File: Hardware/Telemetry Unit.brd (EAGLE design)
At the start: 50.8 x 63.5 mm, 38 parts, among them IC1 MEGA128-A, Q1 10MHz, U1 MPL3115A2, U2 AP65111A, U3 LSM6DS3

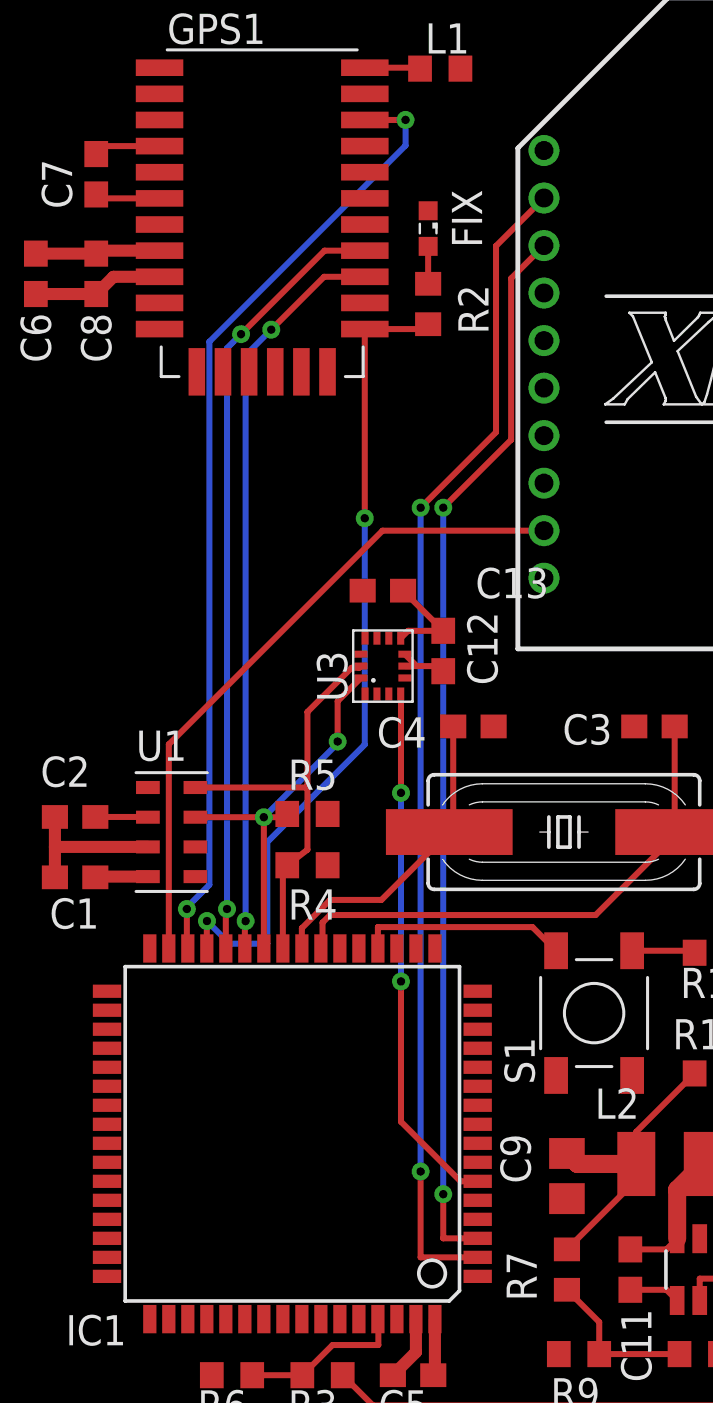
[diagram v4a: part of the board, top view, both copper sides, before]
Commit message: Apparently hadn't completely saved
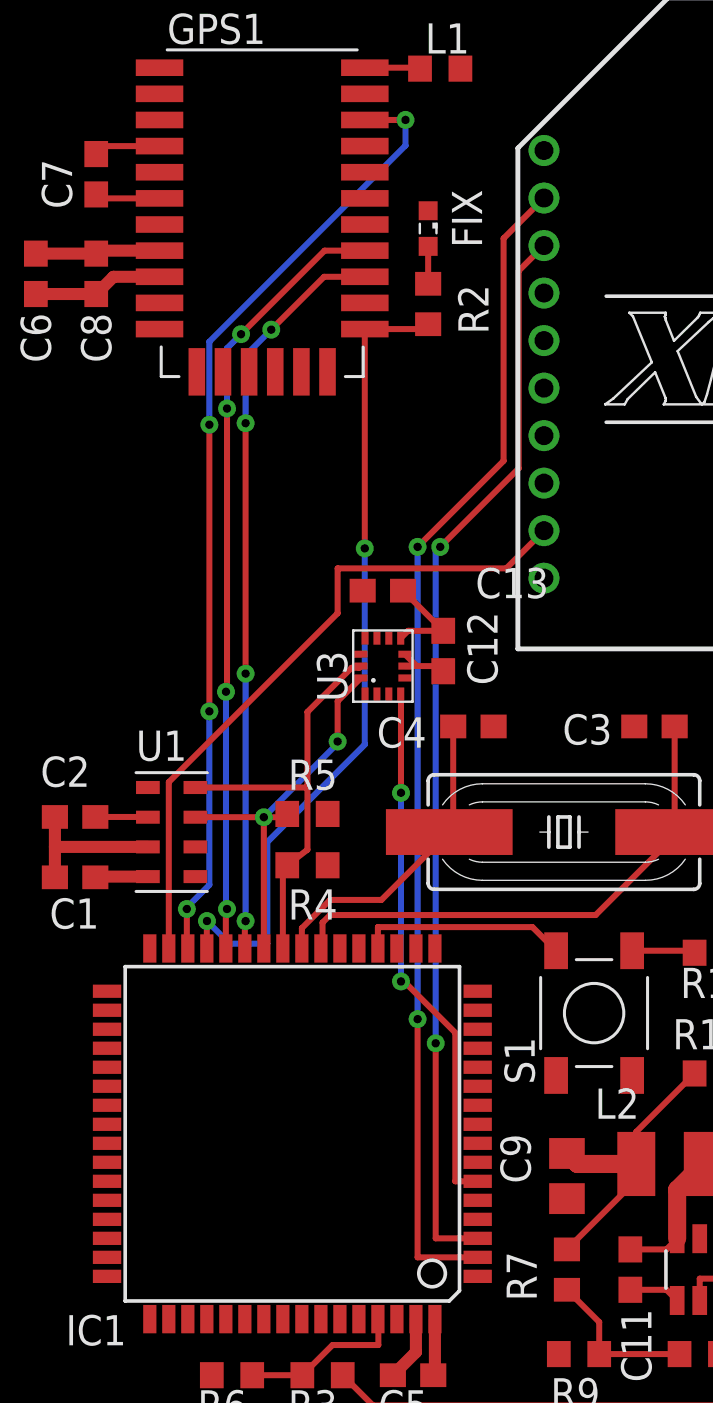
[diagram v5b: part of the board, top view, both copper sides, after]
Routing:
- net TX1: track 32.8 -> 32.9 mm, vias 2 -> 4
- net RX1: vias 2 -> 4
- net !GPS_SLP: vias 2 -> 4
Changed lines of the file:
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@@
 <contactref element="IC1" pad="2"/>
 <contactref element="XB1" pad="2"/>
-<wire x1="20.5" y1="10.04" x2="18.0975" y2="10.04" width="0.254" layer="1"/>
-<wire x1="18.0975" y1="10.04" x2="18.0975" y2="13.6525" width="0.254" layer="1"/>
-<via x="18.0975" y="13.6525" extent="1-16" drill="0.35"/>
-<wire x1="18.0975" y1="13.6525" x2="18.0975" y2="41.5925" width="0.254" layer="16"/>
-<via x="18.0975" y="41.5925" extent="1-16" drill="0.35"/>
-<wire x1="18.0975" y1="41.5925" x2="21.2725" y2="44.7675" width="0.254" layer="1"/>
-<wire x1="21.2725" y1="52.6075" x2="23.29" y2="54.625" width="0.254" layer="1"/>
-<wire x1="21.2725" y1="44.7675" x2="21.2725" y2="52.6075" width="0.254" layer="1"/>
+<wire x1="20.5" y1="10.04" x2="17.9705" y2="10.04" width="0.254" layer="1"/>
+<wire x1="17.9705" y1="10.04" x2="17.9705" y2="20.066" width="0.254" layer="1"/>
+<via x="17.9705" y="20.066" extent="1-16" drill="0.35"/>
+<wire x1="17.9705" y1="39.9415" x2="17.9705" y2="20.066" width="0.254" layer="16"/>
+<via x="17.9705" y="39.9415" extent="1-16" drill="0.35"/>
+<wire x1="17.9705" y1="39.9415" x2="21.59" y2="43.561" width="0.254" layer="1"/>
+<wire x1="21.59" y1="52.925" x2="23.29" y2="54.625" width="0.254" layer="1"/>
+<wire x1="21.59" y1="43.561" x2="21.59" y2="52.925" width="0.254" layer="1"/>
 </signal>
 <signal name="TX0">
 <contactref element="IC1" pad="3"/>
 <contactref element="XB1" pad="3"/>
-<wire x1="20.5" y1="10.84" x2="19.05" y2="10.84" width="0.254" layer="1"/>
-<wire x1="19.05" y1="10.84" x2="19.05" y2="12.7" width="0.254" layer="1"/>
-<via x="19.05" y="12.7" extent="1-16" drill="0.35"/>
-<wire x1="19.05" y1="12.7" x2="19.05" y2="41.5925" width="0.254" layer="16"/>
-<via x="19.05" y="41.5925" extent="1-16" drill="0.35"/>
-<wire x1="19.05" y1="41.5925" x2="21.9075" y2="44.45" width="0.254" layer="1"/>
-<wire x1="21.9075" y1="51.2425" x2="23.29" y2="52.625" width="0.254" layer="1"/>
-<wire x1="21.9075" y1="44.45" x2="21.9075" y2="51.2425" width="0.254" layer="1"/>
+<wire x1="20.5" y1="10.84" x2="18.7325" y2="10.84" width="0.254" layer="1"/>
+<wire x1="18.7325" y1="10.84" x2="18.7325" y2="19.05" width="0.254" layer="1"/>
+<via x="18.7325" y="19.05" extent="1-16" drill="0.35"/>
+<wire x1="18.7325" y1="39.751" x2="18.923" y2="39.9415" width="0.254" layer="16"/>
+<wire x1="18.7325" y1="39.751" x2="18.7325" y2="19.05" width="0.254" layer="16"/>
+<via x="18.923" y="39.9415" extent="1-16" drill="0.35"/>
+<wire x1="18.923" y1="39.9415" x2="22.225" y2="43.2435" width="0.254" layer="1"/>
+<wire x1="22.225" y1="51.56" x2="23.29" y2="52.625" width="0.254" layer="1"/>
+<wire x1="22.225" y1="43.2435" x2="22.225" y2="51.56" width="0.254" layer="1"/>
 </signal>
 <signal name="SCK">
@@
 <wire x1="9.9" y1="24.7015" x2="9.949815625" y2="24.7015" width="0.254" layer="1"/>
 <via x="9.949815625" y="24.7015" extent="1-16" drill="0.35"/>
-<wire x1="9.949815625" y1="24.7015" x2="9.949815625" y2="48.303815625" width="0.254" layer="16"/>
-<wire x1="9.949815625" y1="48.303815625" x2="10.541" y2="48.895" width="0.254" layer="16"/>
+<wire x1="9.949815625" y1="24.7015" x2="9.906" y2="24.745315625" width="0.254" layer="16"/>
+<wire x1="9.906" y1="24.745315625" x2="9.906" y2="33.8455" width="0.254" layer="16"/>
+<wire x1="10.541" y1="48.895" x2="9.949815625" y2="48.303815625" width="0.254" layer="16"/>
+<wire x1="9.949815625" y1="48.303815625" x2="9.949815625" y2="45.763815625" width="0.254" layer="16"/>
 <via x="10.541" y="48.895" extent="1-16" drill="0.35"/>
 <wire x1="10.541" y1="48.895" x2="14.056" y2="52.41" width="0.254" layer="1"/>
 <wire x1="14.056" y1="52.41" x2="15.75" y2="52.41" width="0.254" layer="1"/>
+<via x="9.906" y="33.8455" extent="1-16" drill="0.35"/>
+<via x="9.949815625" y="45.763815625" extent="1-16" drill="0.35"/>
+<wire x1="9.949815625" y1="45.763815625" x2="9.949815625" y2="33.889315625" width="0.254" layer="1"/>
+<wire x1="9.949815625" y1="33.889315625" x2="9.906" y2="33.8455" width="0.254" layer="1"/>
 </signal>
 <signal name="RX1">
@@
 <wire x1="10.7" y1="24.1935" x2="10.7315" y2="24.1935" width="0.254" layer="1"/>
 <via x="10.7315" y="24.1935" extent="1-16" drill="0.35"/>
-<wire x1="10.7315" y1="24.1935" x2="10.7315" y2="48.006" width="0.254" layer="16"/>
-<wire x1="10.7315" y1="48.006" x2="11.811" y2="49.0855" width="0.254" layer="16"/>
+<wire x1="10.7315" y1="24.1935" x2="10.7315" y2="34.6075" width="0.254" layer="16"/>
+<wire x1="10.7315" y1="34.6075" x2="10.7315" y2="45.1485" width="0.254" layer="1"/>
+<wire x1="11.811" y1="49.0855" x2="10.7315" y2="48.006" width="0.254" layer="16"/>
+<wire x1="10.7315" y1="48.006" x2="10.7315" y2="45.1485" width="0.254" layer="16"/>
 <via x="11.811" y="49.0855" extent="1-16" drill="0.35"/>
 <wire x1="15.75" y1="51.31" x2="14.0355" y2="51.31" width="0.254" layer="1"/>
 <wire x1="14.0355" y1="51.31" x2="11.811" y2="49.0855" width="0.254" layer="1"/>
+<via x="10.7315" y="34.6075" extent="1-16" drill="0.35"/>
+<via x="10.7315" y="45.1485" extent="1-16" drill="0.35"/>
 </signal>
 <signal name="MOSI">
@@
 <wire x1="11.6444" y1="23.241" x2="10.0569" y2="23.241" width="0.254" layer="16"/>
 <wire x1="9.1044" y1="24.1935" x2="10.0569" y2="23.241" width="0.254" layer="16"/>
-<wire x1="15.748" y1="31.623" x2="15.748" y2="41.148" width="0.254" layer="16"/>
-<via x="15.748" y="41.148" extent="1-16" drill="0.35"/>
+<wire x1="15.748" y1="31.623" x2="15.748" y2="39.878" width="0.254" layer="16"/>
+<via x="15.748" y="39.878" extent="1-16" drill="0.35"/>
 <wire x1="15.75" y1="49.11" x2="15.748" y2="49.108" width="0.254" layer="1"/>
-<wire x1="15.748" y1="49.108" x2="15.748" y2="41.148" width="0.254" layer="1"/>
+<wire x1="15.748" y1="49.108" x2="15.748" y2="39.878" width="0.254" layer="1"/>
 <wire x1="15.75" y1="49.11" x2="18.21" y2="49.11" width="0.254" layer="1"/>
 <wire x1="18.21" y1="49.11" x2="18.415" y2="49.315" width="0.254" layer="1"/>
@@
 <wire x1="8.2591" y1="24.7015" x2="8.2591" y2="24.7691" width="0.254" layer="16"/>
 <wire x1="8.2591" y1="24.7691" x2="9.2075" y2="25.7175" width="0.254" layer="16"/>
-<wire x1="9.2075" y1="25.7175" x2="9.2075" y2="48.5775" width="0.254" layer="16"/>
-<wire x1="9.2075" y1="48.5775" x2="17.4625" y2="56.8325" width="0.254" layer="16"/>
+<wire x1="9.2075" y1="25.7175" x2="9.2075" y2="33.02" width="0.254" layer="16"/>
+<wire x1="9.2075" y1="33.02" x2="9.2075" y2="45.085" width="0.254" layer="1"/>
+<wire x1="17.4625" y1="56.8325" x2="9.2075" y2="48.5775" width="0.254" layer="16"/>
+<wire x1="9.2075" y1="45.085" x2="9.2075" y2="48.5775" width="0.254" layer="16"/>
 <wire x1="17.4625" y1="56.8325" x2="17.4625" y2="57.912" width="0.254" layer="16"/>
 <via x="17.4625" y="57.912" extent="1-16" drill="0.35"/>
 <wire x1="17.4625" y1="57.912" x2="17.4605" y2="57.91" width="0.254" layer="1"/>
 <wire x1="17.4605" y1="57.91" x2="15.75" y2="57.91" width="0.254" layer="1"/>
+<via x="9.2075" y="33.02" extent="1-16" drill="0.35"/>
+<via x="9.2075" y="45.085" extent="1-16" drill="0.35"/>
 </signal>
 <signal name="RF_SLP">
 <contactref element="XB1" pad="9"/>
 <contactref element="IC1" pad="31"/>
-<wire x1="7.5" y1="23.04" x2="7.5" y2="31.63" width="0.254" layer="1"/>
-<wire x1="16.495" y1="40.625" x2="23.29" y2="40.625" width="0.254" layer="1"/>
-<wire x1="7.5" y1="31.63" x2="16.495" y2="40.625" width="0.254" layer="1"/>
+<wire x1="21.7025" y1="39.0375" x2="23.29" y2="40.625" width="0.254" layer="1"/>
+<wire x1="14.605" y1="39.0375" x2="21.7025" y2="39.0375" width="0.254" layer="1"/>
+<wire x1="7.5" y1="23.04" x2="7.5" y2="30.0425" width="0.254" layer="1"/>
+<wire x1="14.605" y1="37.1475" x2="14.605" y2="39.0375" width="0.254" layer="1"/>
+<wire x1="14.605" y1="37.1475" x2="7.5" y2="30.0425" width="0.254" layer="1"/>
 </signal>
 <signal name="N$5">
@@
 <contactref element="IC1" pad="6"/>
 <contactref element="U3" pad="4"/>
-<wire x1="20.5" y1="13.24" x2="19.78" y2="13.24" width="0.254" layer="1"/>
-<wire x1="17.272" y1="15.748" x2="17.272" y2="21.6535" width="0.254" layer="1"/>
 <via x="17.272" y="21.6535" extent="1-16" drill="0.35"/>
-<wire x1="19.78" y1="13.24" x2="17.272" y2="15.748" width="0.254" layer="1"/>
+<wire x1="20.5" y1="13.24" x2="19.558" y2="13.24" width="0.254" layer="1"/>
+<wire x1="19.558" y1="13.24" x2="19.558" y2="19.4945" width="0.254" layer="1"/>
+<wire x1="19.558" y1="19.4945" x2="17.399" y2="21.6535" width="0.254" layer="1"/>
+<wire x1="17.272" y1="21.6535" x2="17.399" y2="21.6535" width="0.254" layer="1"/>
 <via x="17.272" y="29.591" extent="1-16" drill="0.35"/>
 <wire x1="17.272" y1="29.591" x2="17.272" y2="33.738" width="0.254" layer="1"/>

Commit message: Merging changes into schematics.
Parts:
- added C14: 100nF, rcl:C0603
- added IC2: FT232RL, ftdichip:SSOP28
- added J2: 503182-1852, 503182-1852_SD:MOLEX_503182-1852
- added J3: 10118193-0001LF, 10118193-0001LF_microUSB:FCI_10118193-0001LF
- added LED1, LED2: (no value), led:CHIP-LED0603
- added R12, R13: 1k, rcl:R0603
- added R14: 10k, rcl:R0603
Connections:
- new net CS_SD: IC1.14, J2.1, R14.1
- new net N$11: IC2.16, J3.2
- new net N$13: IC2.15, J3.3
- new net N$15: LED1.C, R12.1
- new net N$16: C14.1, IC2.2
- new net N$17: LED2.C, R13.1
- new net N$18: IC2.22, R12.2
- new net N$19: IC2.23, R13.2
- new net V_USB: J3.1
- net !RST: now also C14.2
- net +3V3: now also J2.4, R14.2
- net GND: now also IC2.18, IC2.19, IC2.21, IC2.25, IC2.26, IC2.7, J2.6, J2.P1, J2.P2, J2.P3, J2.P4, J2.P5, J3.5, J3.S1, J3.S2, J3.S3, J3.S4, J3.S5, J3.S6
- net MISO: now also J2.7
- net MOSI: now also J2.3
- net RX0: now also IC2.1
- net SCK: now also J2.5
- net TX0: now also IC2.5
- net VCC: now also IC2.20, IC2.4, LED1.A, LED2.A

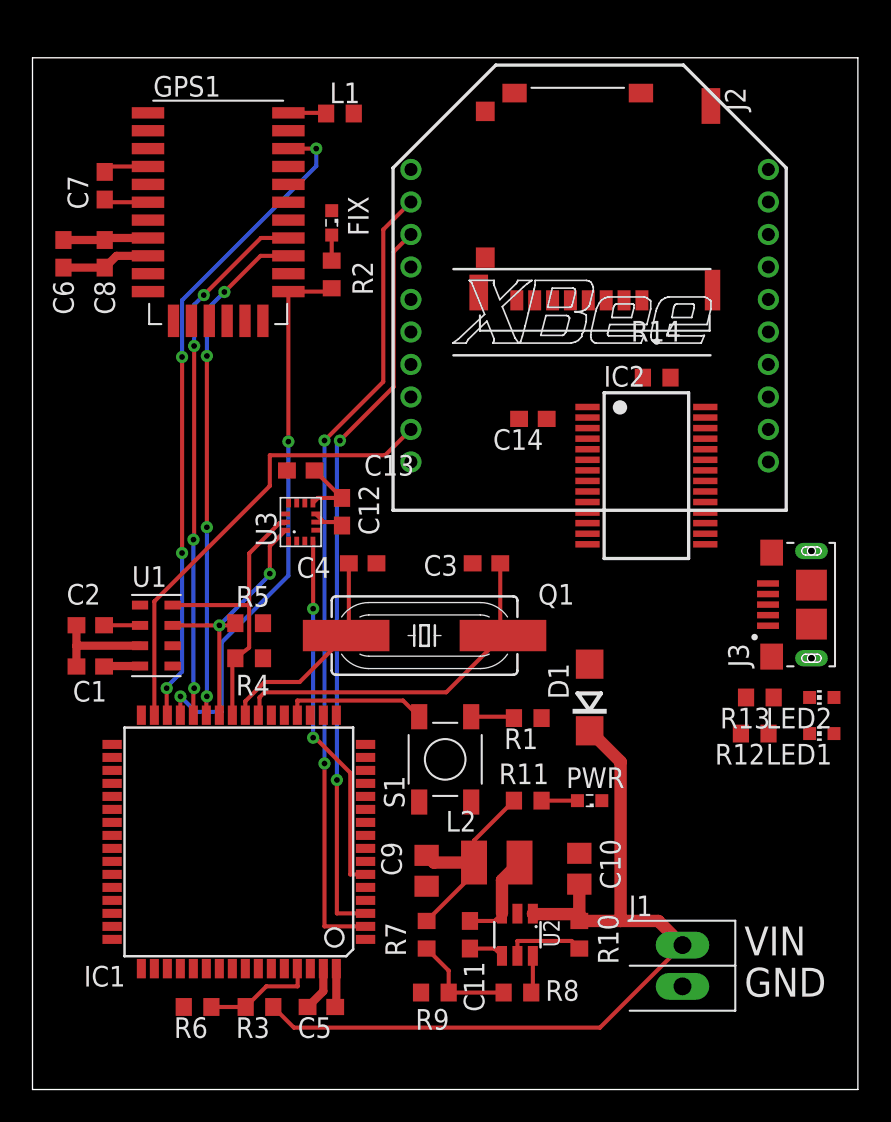
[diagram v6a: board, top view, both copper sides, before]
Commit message: Finished merge, updated layout, added ICSP
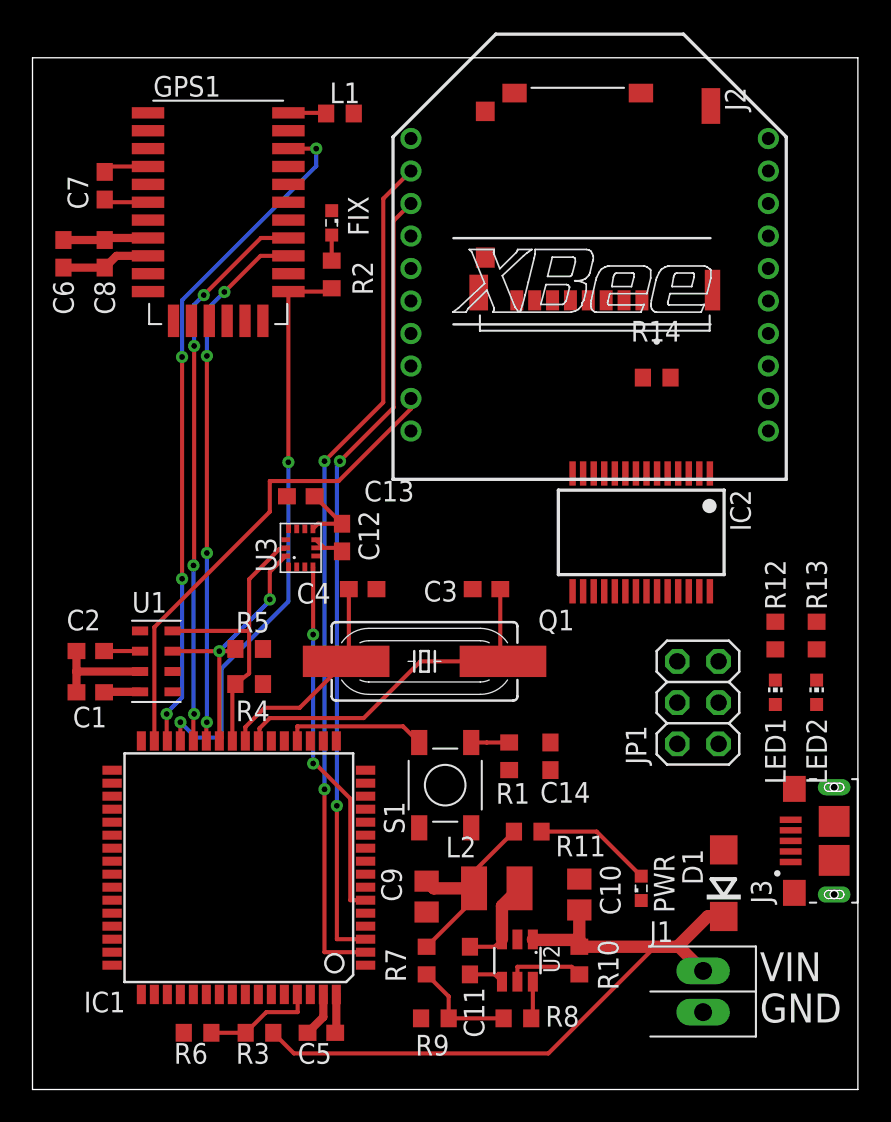
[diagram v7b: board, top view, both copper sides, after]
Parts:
- added JP1: (no value), pinhead:2X03
- moved C14 20.8 mm to (31.9, 20.5), turned to 270 degrees
- moved J3 14.6 mm to (49.3, 15.3)
- moved D1 14.1 mm to (42.5, 12.7)
- moved PWR 6.26 mm to (37.5, 12.4), turned to 90 degrees
- moved R12 6.16 mm to (45.7, 27.9), turned to 90 degrees
- moved R13 5.17 mm to (48.3, 27.9), turned to 90 degrees
- moved LED1 3.82 mm to (45.7, 24.4), turned to 0 degrees
- moved IC2 3.51 mm to (37.5, 34.3), turned to 180 degrees
- moved R1 2.61 mm to (29.3, 20.5), turned to 90 degrees
- moved J1 2.03 mm to (41.3, 6.03)
- moved R11 1.91 mm to (30.5, 15.9)
- moved XB1 1.91 mm to (34.3, 49.5)
- moved C12 1.59 mm to (19.1, 34.0)
- moved Q1 1.59 mm to (24.1, 26.4)
- moved R4 1.59 mm to (13.3, 27.1)
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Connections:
- removed net PROG_PWR: D1.A, XB1.11
- removed net VCC: IC2.20, IC2.4, LED1.A, LED2.A, XB1.1, XB1.5
- net !RST: now also JP1.5; no longer XB1.17
- net +3V3: now also IC2.20, IC2.4, JP1.2, LED1.A, LED2.A, XB1.1, XB1.5
- net GND: now also JP1.6
- net MISO: now also JP1.1; no longer XB1.19
- net MOSI: now also JP1.4; no longer XB1.18
- net SCK: now also JP1.3; no longer XB1.20
- net V_USB: now also D1.A
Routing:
- net VBAT: track 52.4 -> 47.1 mm
- net N$14: track 2.21 -> 7.27 mm
- net TX0: track 45.4 -> 48.9 mm
- net RX0: track 49.3 -> 52.8 mm
- net RF_SLP: track 28.3 -> 30.1 mm
- net TX1: track 32.9 -> 34.4 mm
- net FIX: track 34.5 -> 36.1 mm
- net RX1: track 31.4 -> 33.0 mm
- net !GPS_SLP: track 40.4 -> 42.0 mm

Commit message: Full Routing Complete?
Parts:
- removed LED1, LED2: (no value), led:CHIP-LED0603
- added C15: 2.2u, resistor:C0603
- added R15, R16: 10k, resistor:R0603
- added RX, TX: (no value), led:CHIP-LED0603
- added U$1, U$2, U$3, U$4: (no value), holes:2,8
- moved R14 9.92 mm to (28.6, 45.1)
- moved C5 8.26 mm to (9.53, 3.49), turned to 0 degrees
- moved JP1 3.31 mm to (40.0, 20.6), turned to 270 degrees
- moved R6 3.18 mm to (13.3, 3.49)
- moved R3 3.17 mm to (17.1, 3.49)
- moved J1 2.69 mm to (39.4, 4.13), turned to 270 degrees
- moved R12 1.91 mm to (45.7, 26.0)
- moved R13 1.91 mm to (48.3, 26.0)
- moved D1 1.59 mm to (42.5, 11.1)
- moved IC2 1.59 mm to (37.5, 32.7)
- moved R4 0.32 mm to (13.7, 27.1)
- moved R5 0.32 mm to (13.7, 25.0)
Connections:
- new net N$20: IC2.1, R15.1
- new net N$21: IC2.5, R16.1
- net !RST: no longer C14.2, JP1.5
- net +3V3: now also C15.1, RX.A, TX.A; no longer LED1.A, LED2.A
- net GND: now also C15.2, GPS1.1, S1.P$1
- net N$15: now also RX.C; no longer LED1.C
- net N$17: now also TX.C; no longer LED2.C
- net RST2: now also C14.2, JP1.5
- net RX0: now also R15.2; no longer IC2.1
- net TX0: now also R16.2; no longer IC2.5
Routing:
- net +3V3: track 26.6 -> 271.6 mm, vias 0 -> 8
- net CS_SD: track 0.00 -> 64.5 mm, vias 0 -> 2
- net MOSI: track 0.00 -> 60.3 mm, vias 0 -> 2
- net SCK: track 0.00 -> 55.5 mm, vias 0 -> 2
- net MISO: track 0.00 -> 49.3 mm, vias 0 -> 2
- net N$11: track 0.00 -> 32.4 mm
- net N$13: track 0.00 -> 27.2 mm
- net N$16: track 0.00 -> 24.8 mm
- net RX0: track 52.8 -> 72.1 mm
- net TX0: track 48.9 -> 68.2 mm
- net N$20: track 0.00 -> 12.6 mm
- net N$19: track 0.00 -> 11.2 mm
- net RST2: track 2.34 -> 13.1 mm
- net GND: track 17.1 -> 26.7 mm, vias 0 -> 38
- net N$18: track 0.00 -> 9.33 mm
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- added copper zone on layer 1, net GND
- added copper zone on layer 16, net GND
